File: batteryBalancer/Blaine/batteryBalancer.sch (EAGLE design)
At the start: 36 parts

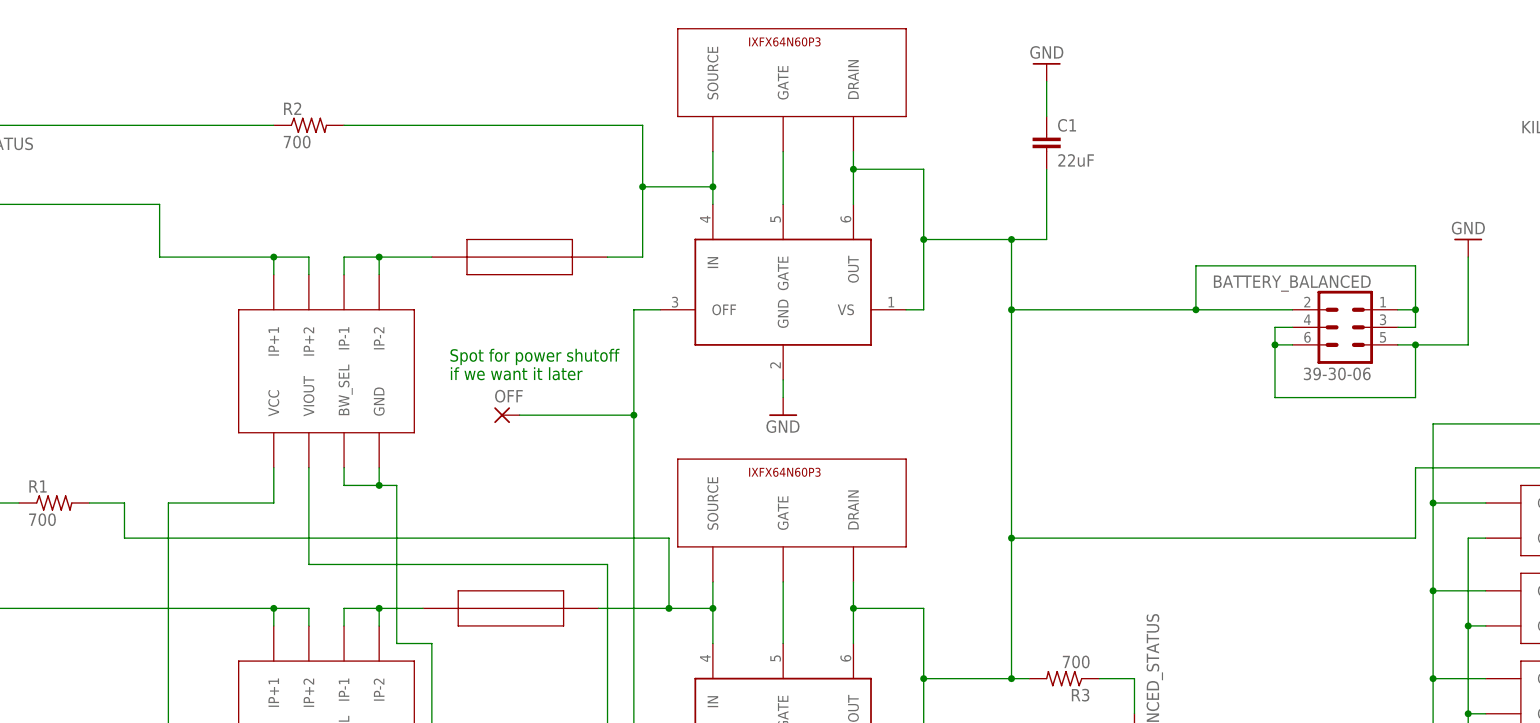
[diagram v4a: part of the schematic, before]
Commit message: Added testpoints
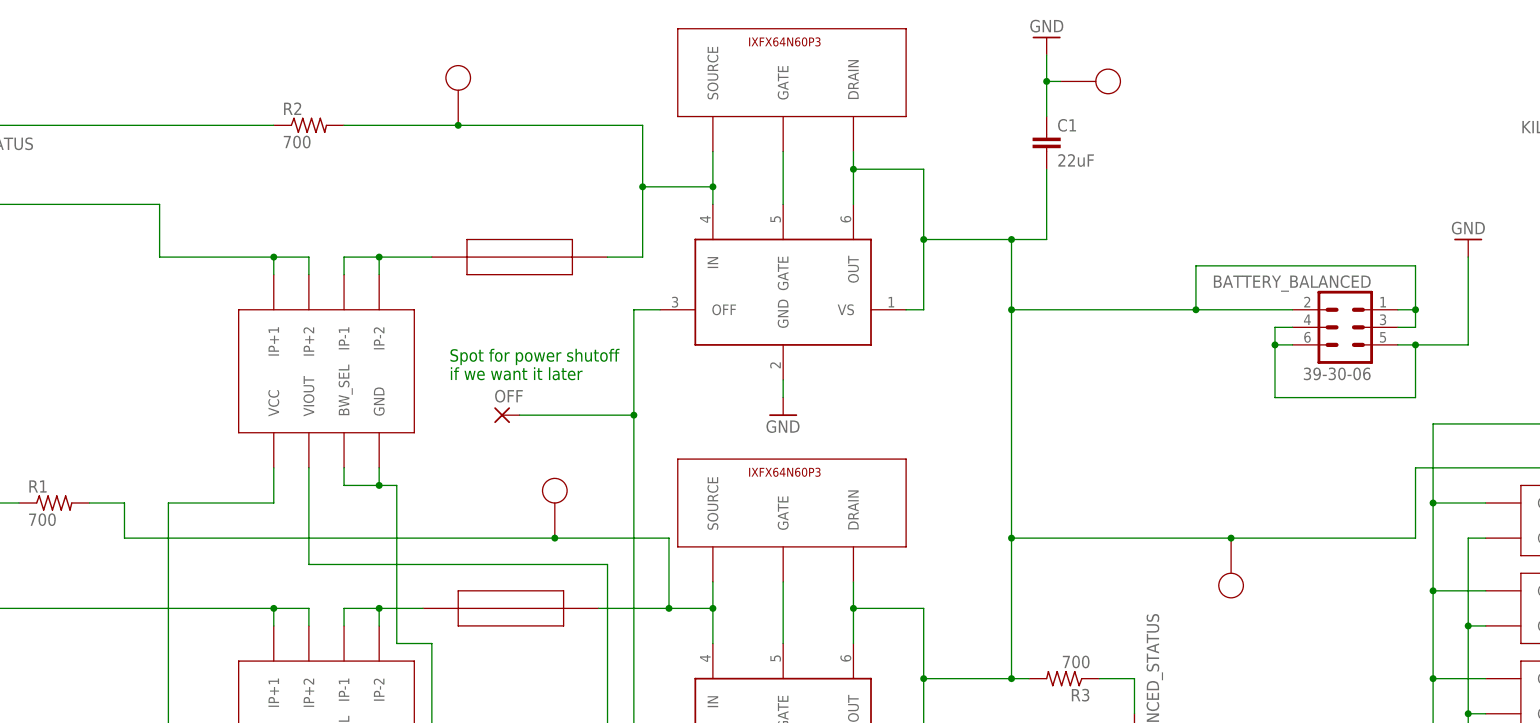
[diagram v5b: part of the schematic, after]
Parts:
- added U$1, U$2, U$3, U$4: 5010_C, 5010_c:5010_C
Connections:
- net BALANCED_POWER: now also U$3.P$1
- net GND: now also U$4.P$1
- net PORT_SOURCE: now also U$2.P$1
- net STBD_UNBALANCED: now also U$1.P$1
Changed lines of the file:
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@@
 <layer number="59" name="tCarbon" color="7" fill="1" visible="no" active="no"/>
 <layer number="60" name="bCarbon" color="7" fill="1" visible="no" active="no"/>
+<layer number="88" name="SimResults" color="9" fill="1" visible="yes" active="yes"/>
+<layer number="89" name="SimProbes" color="9" fill="1" visible="yes" active="yes"/>
 <layer number="90" name="Modules" color="5" fill="1" visible="yes" active="yes"/>
 <layer number="91" name="Nets" color="2" fill="1" visible="yes" active="yes"/>
@@
 <part name="C2" library="SparkFun-Capacitors" deviceset="0.1UF" device="-KIT-EZ-50V-20%" value="0.1uF"/>
 <part name="C3" library="SparkFun-Capacitors" deviceset="0.1UF" device="-KIT-EZ-50V-20%" value="0.1uF"/>
+<part name="U$1" library="5010_c" deviceset="5010_C" device=""/>
+<part name="U$2" library="5010_c" deviceset="5010_C" device=""/>
+<part name="U$3" library="5010_c" deviceset="5010_C" device=""/>
+<part name="U$4" library="5010_c" deviceset="5010_C" device=""/>
 </parts>
 <sheets>
@@
 <instance part="R2" gate="G$1" x="119.38" y="224.79"/>
 <instance part="C1" gate="G$1" x="226.06" y="220.98"/>
-<instance part="GND4" gate="1" x="226.06" y="233.68" rot="R180"/>
+<instance part="GND4" gate="1" x="226.06" y="237.49" rot="R180"/>
 <instance part="R3" gate="G$1" x="228.6" y="144.78" rot="R180"/>
 <instance part="GND6" gate="1" x="238.76" y="124.46"/>
@@
 <instance part="C2" gate="G$1" x="170.18" y="124.46" rot="R90"/>
 <instance part="C3" gate="G$1" x="176.53" y="118.11" rot="R90"/>
+<instance part="U$1" gate="G$1" x="140.97" y="231.648" rot="R90"/>
+<instance part="U$2" gate="G$1" x="154.94" y="171.958" rot="R90"/>
+<instance part="U$3" gate="G$1" x="252.73" y="158.242" rot="R270"/>
+<instance part="U$4" gate="G$1" x="234.95" y="231.14"/>
 </instances>
 <busses>
@@
 <pinref part="GND4" gate="1" pin="GND"/>
 <wire x1="226.06" y1="226.06" x2="226.06" y2="231.14" width="0.1524" layer="91"/>
+<pinref part="U$4" gate="G$1" pin="P$1"/>
+<wire x1="226.06" y1="231.14" x2="226.06" y2="234.95" width="0.1524" layer="91"/>
+<wire x1="226.06" y1="231.14" x2="228.092" y2="231.14" width="0.1524" layer="91"/>
+<junction x="226.06" y="231.14"/>
 </segment>
 <segment>
@@
 <junction x="167.64" y="215.9"/>
 <pinref part="R2" gate="G$1" pin="2"/>
-<wire x1="167.64" y1="224.79" x2="124.46" y2="224.79" width="0.1524" layer="91"/>
+<wire x1="167.64" y1="224.79" x2="140.97" y2="224.79" width="0.1524" layer="91"/>
+<pinref part="U$1" gate="G$1" pin="P$1"/>
+<wire x1="140.97" y1="224.79" x2="124.46" y2="224.79" width="0.1524" layer="91"/>
+<junction x="140.97" y="224.79"/>
 </segment>
 </net>
@@
 <junction x="220.98" y="198.12"/>
 <wire x1="247.65" y1="198.12" x2="220.98" y2="198.12" width="0.1524" layer="91"/>
-<wire x1="220.98" y1="165.1" x2="279.4" y2="165.1" width="0.1524" layer="91"/>
+<wire x1="220.98" y1="165.1" x2="252.73" y2="165.1" width="0.1524" layer="91"/>
 <junction x="220.98" y="165.1"/>
 <pinref part="STBD_FET" gate="G$1" pin="DRAIN"/>
+<wire x1="252.73" y1="165.1" x2="279.4" y2="165.1" width="0.1524" layer="91"/>
 <wire x1="198.12" y1="220.98" x2="198.12" y2="218.44" width="0.1524" layer="91"/>
 <junction x="198.12" y="218.44"/>
@@
 <junction x="345.44" y="170.18"/>
 <junction x="247.65" y="198.12"/>
+<pinref part="U$3" gate="G$1" pin="P$1"/>
+<junction x="252.73" y="165.1"/>
 </segment>
 </net>
@@
 <wire x1="171.45" y1="154.94" x2="177.8" y2="154.94" width="0.1524" layer="91"/>
 <wire x1="92.71" y1="170.18" x2="92.71" y2="165.1" width="0.1524" layer="91"/>
-<wire x1="92.71" y1="165.1" x2="171.45" y2="165.1" width="0.1524" layer="91"/>
+<wire x1="92.71" y1="165.1" x2="154.94" y2="165.1" width="0.1524" layer="91"/>
+<wire x1="154.94" y1="165.1" x2="171.45" y2="165.1" width="0.1524" layer="91"/>
 <wire x1="171.45" y1="165.1" x2="171.45" y2="154.94" width="0.1524" layer="91"/>
 <junction x="171.45" y="154.94"/>
 <pinref part="R1" gate="G$1" pin="2"/>
 <wire x1="92.71" y1="170.18" x2="87.63" y2="170.18" width="0.1524" layer="91"/>
-</segment>
-</net>
+<pinref part="U$2" gate="G$1" pin="P$1"/>
+<junction x="154.94" y="165.1"/>
+</segment>
+</net>

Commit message: Done, made gerbers, time for lunch
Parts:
- renumbered KILL_SWITCH_CONNECTOR to KILL_SWITCH
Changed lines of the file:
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@@
 <part name="EDGE_CONNECTOR" library="5530843-6" deviceset="5530843" device=""/>
 <part name="OFF" library="wirepad" library_urn="urn:adsk.eagle:library:412" deviceset="2,54/1,1" device="" package3d_urn="urn:adsk.eagle:package:30836/1"/>
-<part name="KILL_SWITCH_CONNECTOR" library="con-molex-mini-fit" deviceset="39-30-?02?" device=""/>
 <part name="R8" library="rcl" library_urn="urn:adsk.eagle:library:334" deviceset="R-US_" device="0207/7" package3d_urn="urn:adsk.eagle:package:23493/1" value="700"/>
 <part name="KILL_STATUS" library="LTST-S270GKT" deviceset="LTST-S270GKT" device=""/>
@@
 <part name="U$3" library="5010_c" deviceset="5010_C" device=""/>
 <part name="U$4" library="5010_c" deviceset="5010_C" device=""/>
+<part name="KILL_SWITCH" library="con-molex-mini-fit" deviceset="39-30-?02?" device=""/>
 </parts>
 <sheets>
@@
 <instance part="EDGE_CONNECTOR" gate="G$1" x="275.59" y="67.31" rot="R180"/>
 <instance part="OFF" gate="1" x="147.32" y="182.88"/>
-<instance part="KILL_SWITCH_CONNECTOR" gate="G$1" x="308.61" y="228.6" smashed="yes" rot="MR180">
-<attribute name="NAME" x="294.64" y="225.425" size="1.778" layer="95" rot="MR180"/>
-<attribute name="VALUE" x="304.8" y="233.68" size="1.778" layer="95" rot="MR180"/>
-</instance>
 <instance part="R8" gate="G$1" x="265.43" y="129.54" rot="R180"/>
 <instance part="KILL_STATUS" gate="G$1" x="255.27" y="125.73"/>
@@
 <instance part="U$3" gate="G$1" x="252.73" y="158.242" rot="R270"/>
 <instance part="U$4" gate="G$1" x="234.95" y="231.14"/>
+<instance part="KILL_SWITCH" gate="G$1" x="308.61" y="228.6" smashed="yes" rot="MR180">
+<attribute name="NAME" x="294.64" y="225.425" size="1.778" layer="95" rot="MR180"/>
+<attribute name="VALUE" x="304.8" y="233.68" size="1.778" layer="95" rot="MR180"/>
+</instance>
 </instances>
 <busses>
@@
 <wire x1="403.86" y1="106.68" x2="403.86" y2="228.6" width="0.1524" layer="91"/>
 <junction x="341.63" y="106.68"/>
-<pinref part="KILL_SWITCH_CONNECTOR" gate="G$1" pin="2"/>
 <wire x1="403.86" y1="228.6" x2="316.23" y2="228.6" width="0.1524" layer="91"/>
 <pinref part="EDGE_CONNECTOR" gate="G$1" pin="3.3V_6"/>
@@
 <pinref part="R7" gate="G$1" pin="2"/>
 <wire x1="114.3" y1="58.42" x2="116.84" y2="58.42" width="0.1524" layer="91"/>
+<pinref part="KILL_SWITCH" gate="G$1" pin="2"/>
 </segment>
 </net>
@@
 <wire x1="281.94" y1="181.61" x2="281.94" y2="170.18" width="0.1524" layer="91"/>
 <junction x="281.94" y="170.18"/>
-<pinref part="KILL_SWITCH_CONNECTOR" gate="G$1" pin="1"/>
 <wire x1="281.94" y1="181.61" x2="300.99" y2="181.61" width="0.1524" layer="91"/>
 <wire x1="300.99" y1="181.61" x2="300.99" y2="228.6" width="0.1524" layer="91"/>
@@
 <wire x1="270.51" y1="129.54" x2="281.94" y2="129.54" width="0.1524" layer="91"/>
 <junction x="281.94" y="129.54"/>
+<pinref part="KILL_SWITCH" gate="G$1" pin="1"/>
 </segment>
 </net>
@@
 </sheet>
 </sheets>
+<errors>
+</errors>
 </schematic>
 </drawing>

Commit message: Added battery gnd to backplane
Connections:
- net BALANCED_POWER: now also EDGE_CONNECTOR.EXTRA1, EDGE_CONNECTOR.EXTRA23
- net GND: now also EDGE_CONNECTOR.EXTRA2, EDGE_CONNECTOR.EXTRA24
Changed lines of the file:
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@@
 <part name="U$4" library="5010_c" deviceset="5010_C" device=""/>
 <part name="KILL_SWITCH" library="con-molex-mini-fit" deviceset="39-30-?02?" device=""/>
+<part name="GND10" library="supply1" library_urn="urn:adsk.eagle:library:371" deviceset="GND" device=""/>
+<part name="GND11" library="supply1" library_urn="urn:adsk.eagle:library:371" deviceset="GND" device=""/>
 </parts>
 <sheets>
@@
 <attribute name="VALUE" x="304.8" y="233.68" size="1.778" layer="95" rot="MR180"/>
 </instance>
+<instance part="GND10" gate="1" x="306.07" y="27.94"/>
+<instance part="GND11" gate="1" x="255.27" y="97.79" rot="R180"/>
 </instances>
 <busses>
@@
 <pinref part="GND8" gate="1" pin="GND"/>
 <wire x1="393.7" y1="160.02" x2="393.7" y2="177.8" width="0.1524" layer="91"/>
+</segment>
+<segment>
+<pinref part="EDGE_CONNECTOR" gate="G$1" pin="EXTRA2"/>
+<wire x1="306.07" y1="46.99" x2="306.07" y2="30.48" width="0.1524" layer="91"/>
+<pinref part="GND10" gate="1" pin="GND"/>
+</segment>
+<segment>
+<pinref part="EDGE_CONNECTOR" gate="G$1" pin="EXTRA24"/>
+<pinref part="GND11" gate="1" pin="GND"/>
+<wire x1="255.27" y1="90.17" x2="255.27" y2="95.25" width="0.1524" layer="91"/>
 </segment>
 </net>
@@
 <wire x1="208.28" y1="144.78" x2="208.28" y2="134.62" width="0.1524" layer="91"/>
 <wire x1="208.28" y1="134.62" x2="205.74" y2="134.62" width="0.1524" layer="91"/>
-<wire x1="220.98" y1="144.78" x2="208.28" y2="144.78" width="0.1524" layer="91"/>
+<wire x1="220.98" y1="144.78" x2="214.63" y2="144.78" width="0.1524" layer="91"/>
 <junction x="208.28" y="144.78"/>
 <pinref part="C1" gate="G$1" pin="2"/>
+<wire x1="214.63" y1="144.78" x2="208.28" y2="144.78" width="0.1524" layer="91"/>
 <wire x1="220.98" y1="208.28" x2="226.06" y2="208.28" width="0.1524" layer="91"/>
 <wire x1="226.06" y1="208.28" x2="226.06" y2="218.44" width="0.1524" layer="91"/>
@@
 <pinref part="U$3" gate="G$1" pin="P$1"/>
 <junction x="252.73" y="165.1"/>
-</segment>
-</net>
+<wire x1="214.63" y1="144.78" x2="214.63" y2="119.38" width="0.1524" layer="91"/>
+<junction x="214.63" y="144.78"/>
+<pinref part="EDGE_CONNECTOR" gate="G$1" pin="EXTRA23"/>
+<wire x1="214.63" y1="119.38" x2="260.35" y2="119.38" width="0.1524" layer="91"/>
+<wire x1="260.35" y1="119.38" x2="260.35" y2="90.17" width="0.1524" layer="91"/>
+<wire x1="260.35" y1="119.38" x2="364.49" y2="119.38" width="0.1524" layer="91"/>
+<wire x1="364.49" y1="119.38" x2="364.49" y2="30.48" width="0.1524" layer="91"/>
+<junction x="260.35" y="119.38"/>
+<pinref part="EDGE_CONNECTOR" gate="G$1" pin="EXTRA1"/>
+<wire x1="311.15" y1="46.99" x2="311.15" y2="30.48" width="0.1524" layer="91"/>
+<wire x1="364.49" y1="30.48" x2="311.15" y2="30.48" width="0.1524" layer="91"/>
+</segment>
+</net>
